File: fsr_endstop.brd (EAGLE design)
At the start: 55.9 x 38.1 mm, 32 parts, among them U1 ATTINY461

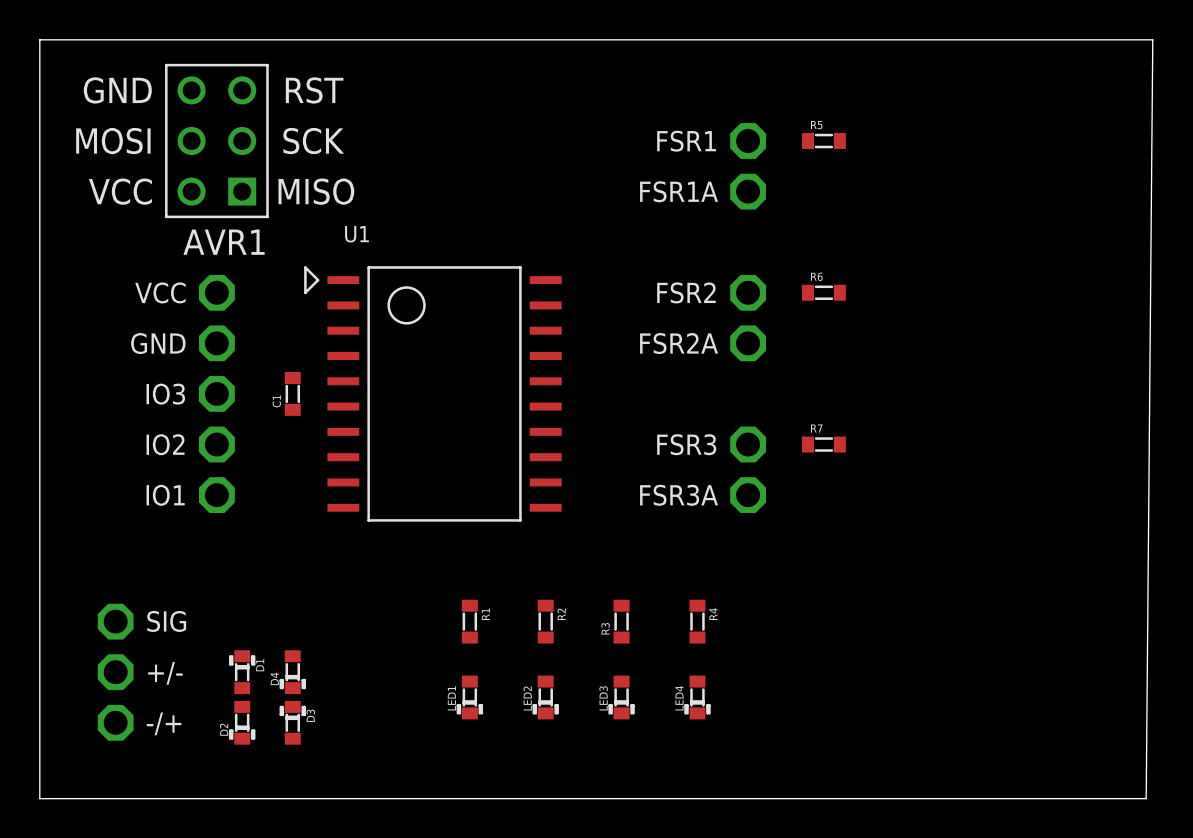
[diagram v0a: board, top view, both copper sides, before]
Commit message: Packed components in tighter
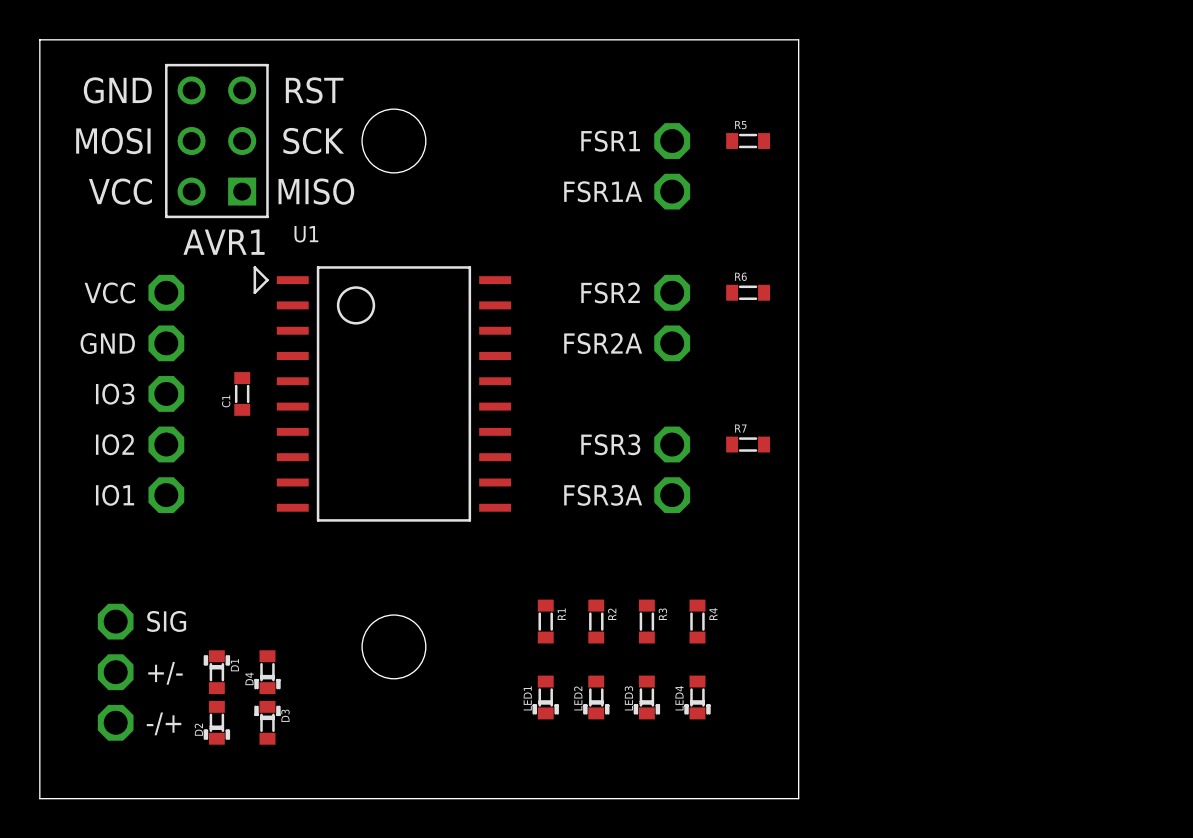
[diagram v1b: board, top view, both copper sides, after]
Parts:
- moved LED1 3.81 mm to (38.1, 17.8)
- moved R1 3.81 mm to (38.1, 21.6)
- moved R5 3.81 mm to (48.3, 45.7)
- moved R6 3.81 mm to (48.3, 38.1)
- moved R7 3.81 mm to (48.3, 30.5)
- moved FSR1 3.81 mm to (44.5, 45.7)
- moved FSR1A 3.81 mm to (44.5, 43.2)
- moved FSR2 3.81 mm to (44.5, 38.1)
- moved FSR2A 3.81 mm to (44.5, 35.6)
- moved FSR3 3.81 mm to (44.5, 30.5)
- moved FSR3A 3.81 mm to (44.5, 27.9)
- moved U1 2.54 mm to (30.5, 33.0)
- moved C1 2.54 mm to (22.9, 33.0)
- moved GND 2.54 mm to (19.1, 35.6)
- moved IO1 2.54 mm to (19.1, 27.9)
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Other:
- board size 55.9 x 38.1 mm -> 38.1 x 38.1 mm

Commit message: Completed routing
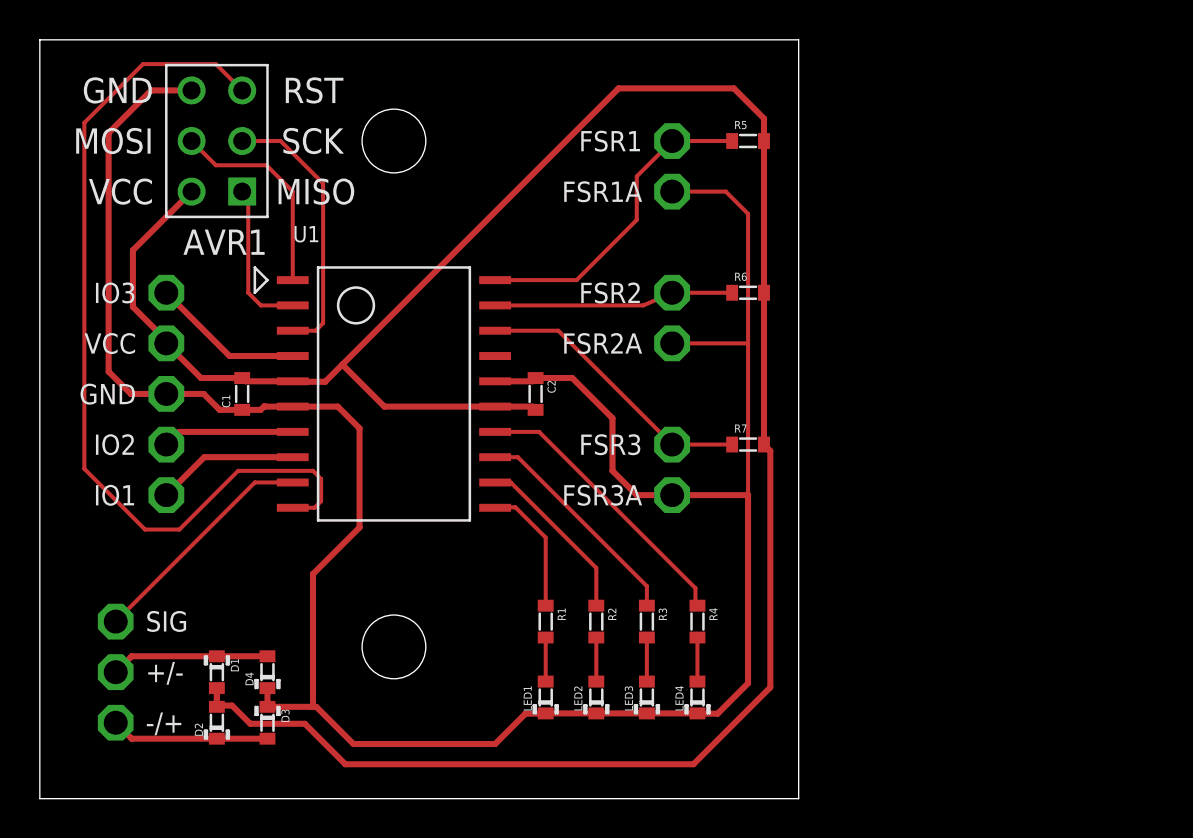
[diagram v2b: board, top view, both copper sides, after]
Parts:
- added C2: 1uF, _sg_lib:0603
- moved IO3 5.08 mm to (19.1, 38.1)
- moved GND 2.54 mm to (19.1, 33.0)
- moved VCC 2.54 mm to (19.1, 35.6)
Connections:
- net GND: now also C2.1
- net N$14: now also U1.P$9; no longer U1.P$4
- net N$15: now also IO3.P$1, U1.P$4; no longer IO1.P$1, U1.P$9
- net N$16: now also IO1.P$1; no longer IO2.P$1
- net N$17: now also IO2.P$1; no longer IO3.P$1
- net V+: now also C2.2
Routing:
- net GND: track 0.00 -> 121.5 mm
- net V+: track 0.00 -> 118.9 mm
- net N$6: track 0.00 -> 44.3 mm
- net N$7: track 0.00 -> 16.1 mm
- net N$9: track 0.00 -> 14.3 mm
- net N$10: track 0.00 -> 14.2 mm
- net N$5: track 0.00 -> 13.6 mm
- net N$8: track 0.00 -> 12.0 mm
- net N$14: track 0.00 -> 11.8 mm
- net N$11: track 0.00 -> 11.3 mm
- net N$1: track 0.00 -> 10.6 mm
- net N$12: track 0.00 -> 8.75 mm
- net N$4: track 0.00 -> 7.95 mm
- net N$3: track 0.00 -> 7.95 mm
- net N$2: track 0.00 -> 7.70 mm
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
